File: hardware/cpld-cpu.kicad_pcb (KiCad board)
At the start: 4 copper layers, 264.2 x 190.5 mm, 386 parts, among them J1 Acc, J10 Page, J11 PC_H, J12 Conn_02x16_Odd_Even, J13 Page, J14 Conn_02x16_Odd_Even, J2 X, J3 IR, J4 AXM, J5 Dec, J6 AR, J7 ALU, J8 Index, J9 PC_L, SW1 BTN0, SW2 BTN0, SW3 BTN0, U1 Acc, U10 RAM_Page, U11 PC_H, U12 CY62138FV30LL, U13 GPIO_RNG, U2 X, U3 IR, U4 Multiplexer, U5 Decoder, U6 AR, U7 ALU, U8 RAM_Index, U9 PC_L

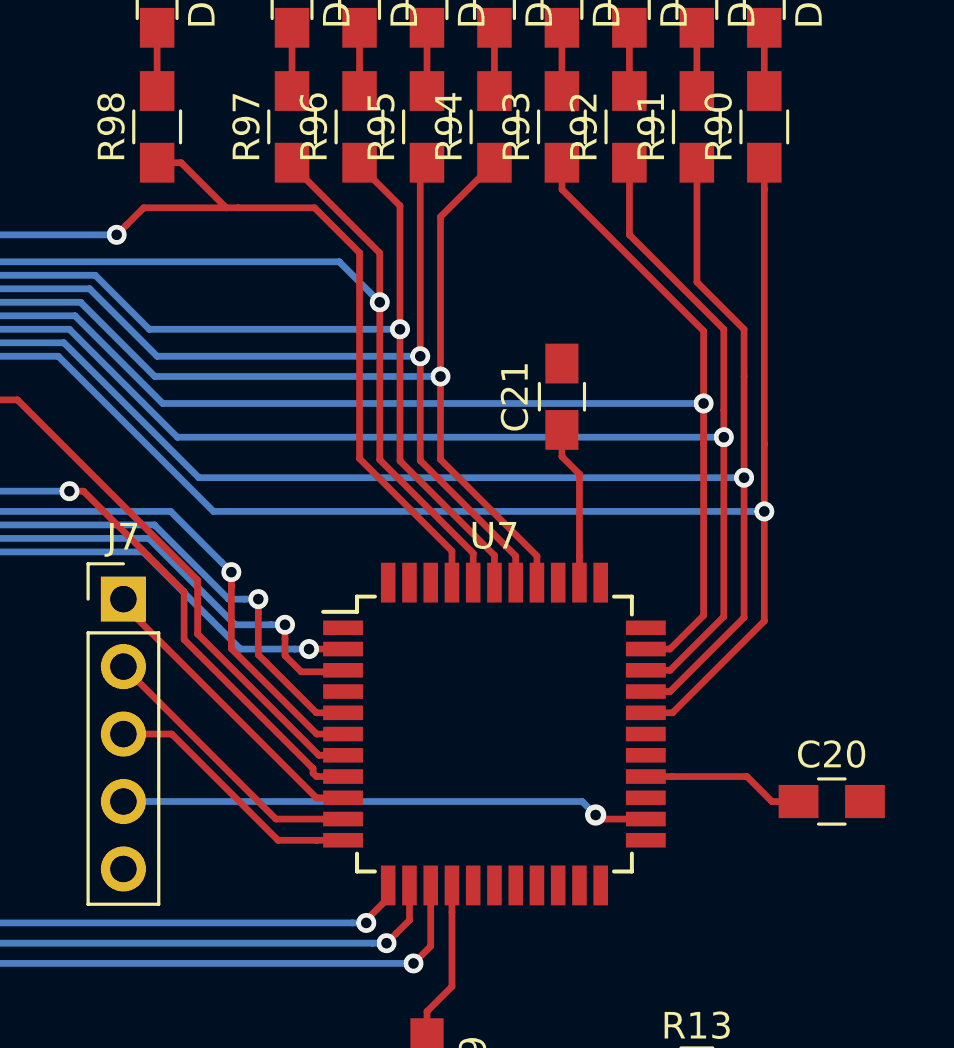
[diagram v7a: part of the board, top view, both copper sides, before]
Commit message: VHDL for alu/decoder/multiplexer
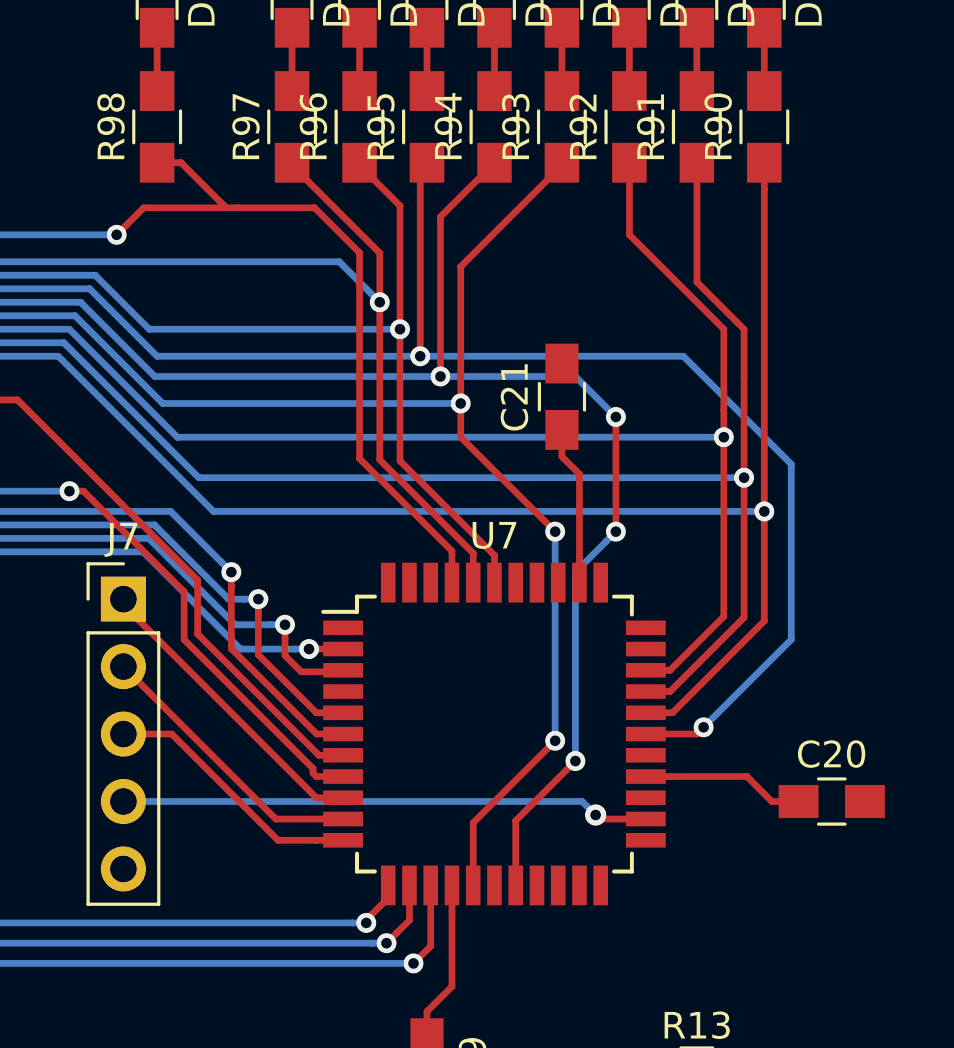
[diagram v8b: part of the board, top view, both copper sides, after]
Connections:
- U7 pad 16: /D0 -> /ALU3
- U7 pad 18: /D1 -> /ALU4
- U7 pad 28: /IR5 -> /ALU5
- U7 pad 32: /ALU3 -> /IR5
- U7 pad 37: /ALU4 -> /D0
- U7 pad 38: /ALU5 -> /D1
- U7 pad 43: /ALU_OE -> /ALU_WE
- U7 pad 44: /ALU_WE -> /ALU_OE
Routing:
- net /ALU5: track 199.3 -> 218.5 mm, vias 4 -> 5
- net /ALU4: track 198.1 -> 215.2 mm, vias 4 -> 7
- net /ALU3: track 209.4 -> 209.9 mm, vias 4 -> 6
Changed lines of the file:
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@@
     (thickness 1.6)
     (drawings 142)
-    (tracks 1644)
+    (tracks 1659)
     (zones 0)
     (modules 386)
@@
       (net 2 VCC))
     (pad 16 smd rect (at -0.8 5.7 90) (size 1.5 0.55) (layers F.Cu F.Paste F.Mask)
-      (net 125 /D0))
+      (net 165 /ALU3))
     (pad 17 smd rect (at 0 5.7 90) (size 1.5 0.55) (layers F.Cu F.Paste F.Mask)
       (net 1 GND))
     (pad 18 smd rect (at 0.8 5.7 90) (size 1.5 0.55) (layers F.Cu F.Paste F.Mask)
-      (net 124 /D1))
+      (net 166 /ALU4))
     (pad 19 smd rect (at 1.6 5.7 90) (size 1.5 0.55) (layers F.Cu F.Paste F.Mask)
       (net 126 /D2))
@@
       (net 131 /D7))
     (pad 28 smd rect (at 5.7 0) (size 1.5 0.55) (layers F.Cu F.Paste F.Mask)
-      (net 104 /IR5))
+      (net 167 /ALU5))
     (pad 29 smd rect (at 5.7 -0.8) (size 1.5 0.55) (layers F.Cu F.Paste F.Mask)
       (net 162 /ALU0))
@@
       (net 164 /ALU2))
     (pad 32 smd rect (at 5.7 -3.2) (size 1.5 0.55) (layers F.Cu F.Paste F.Mask)
-      (net 165 /ALU3))
+      (net 104 /IR5))
     (pad 33 smd rect (at 5.7 -4) (size 1.5 0.55) (layers F.Cu F.Paste F.Mask)
       (net 171 /RST))
@@
       (net 461 "Net-(U7-Pad36)"))
     (pad 37 smd rect (at 1.6 -5.7 90) (size 1.5 0.55) (layers F.Cu F.Paste F.Mask)
-      (net 166 /ALU4))
+      (net 125 /D0))
     (pad 38 smd rect (at 0.8 -5.7 90) (size 1.5 0.55) (layers F.Cu F.Paste F.Mask)
-      (net 167 /ALU5))
+      (net 124 /D1))
     (pad 39 smd rect (at 0 -5.7 90) (size 1.5 0.55) (layers F.Cu F.Paste F.Mask)
       (net 168 /ALU6))
@@
       (net 462 "Net-(U7-Pad42)"))
     (pad 43 smd rect (at -3.2 -5.7 90) (size 1.5 0.55) (layers F.Cu F.Paste F.Mask)
-      (net 192 /ALU_OE))
-    (pad 44 smd rect (at -4 -5.7 90) (size 1.5 0.55) (layers F.Cu F.Paste F.Mask)
       (net 191 /ALU_WE))
+    (pad 44 smd rect (at -4 -5.7 90) (size 1.5 0.55) (layers F.Cu F.Paste F.Mask)
+      (net 192 /ALU_OE))
     (model ${KISYS3DMOD}/Housings_QFP.3dshapes/TQFP-44_10x10mm_Pitch0.8mm.wrl
       (at (xyz 0 0 0))
@@
   (segment (start 32.4 120.976001) (end 32.4 121.12) (width 0.254) (layer F.Cu) (net 164))
   (segment (start 28.956 118.586802) (end 31.345199 120.976001) (width 0.254) (layer F.Cu) (net 164))
-  (segment (start 121.922916 37.914) (end 121.922916 36.91) (width 0.254) (layer F.Cu) (net 165))
-  (segment (start 127.254 43.245084) (end 121.922916 37.914) (width 0.254) (layer F.Cu) (net 165))
-  (segment (start 125.08 55.22) (end 125.990802 55.22) (width 0.254) (layer F.Cu) (net 165))
-  (segment (start 125.990802 55.22) (end 127.254 53.956802) (width 0.254) (layer F.Cu) (net 165))
-  (via (at 127.254 45.974) (size 0.75) (drill 0.4) (layers F.Cu B.Cu) (net 165))
-  (segment (start 127.254 47.244) (end 127.254 47.498) (width 0.254) (layer F.Cu) (net 165))
-  (segment (start 127.254 47.244) (end 127.254 43.245084) (width 0.254) (layer F.Cu) (net 165))
-  (segment (start 127.254 53.956802) (end 127.254 47.498) (width 0.254) (layer F.Cu) (net 165))
-  (segment (start 106.890432 45.974) (end 103.588412 42.67198) (width 0.254) (layer B.Cu) (net 165))
-  (segment (start 29.107136 42.671982) (end 28.267389 43.511729) (width 0.254) (layer B.Cu) (net 165))
-  (segment (start 103.588412 42.67198) (end 29.107136 42.671982) (width 0.254) (layer B.Cu) (net 165))
-  (segment (start 28.267389 43.616744) (end 28.267389 44.147074) (width 0.254) (layer B.Cu) (net 165))
   (via (at 28.267389 44.147074) (size 0.75) (drill 0.4) (layers F.Cu B.Cu) (net 165))
-  (segment (start 28.267389 43.511729) (end 28.267389 43.616744) (width 0.254) (layer B.Cu) (net 165))
-  (segment (start 127.254 45.974) (end 106.890432 45.974) (width 0.254) (layer B.Cu) (net 165))
   (segment (start 28.429444 44.309129) (end 28.267389 44.147074) (width 0.254) (layer F.Cu) (net 165))
   (segment (start 28.429444 45.354696) (end 28.429444 44.309129) (width 0.254) (layer F.Cu) (net 165))
@@
   (segment (start 31.268999 121.484011) (end 31.134775 121.484011) (width 0.254) (layer F.Cu) (net 165))
   (segment (start 32.256001 121.776001) (end 31.345199 121.776001) (width 0.254) (layer F.Cu) (net 165))
-  (segment (start 120.98 51.716) (end 120.98 52.72) (width 0.254) (layer F.Cu) (net 166))
-  (segment (start 117.348 48.084) (end 120.98 51.716) (width 0.254) (layer F.Cu) (net 166))
+  (segment (start 28.267389 43.616744) (end 28.267389 44.147074) (width 0.254) (layer B.Cu) (net 165))
+  (segment (start 118.11 45.974) (end 106.890432 45.974) (width 0.254) (layer B.Cu) (net 165))
+  (segment (start 106.890432 45.974) (end 103.588412 42.67198) (width 0.254) (layer B.Cu) (net 165))
+  (via (at 118.11 45.974) (size 0.75) (drill 0.4) (layers F.Cu B.Cu) (net 165))
+  (segment (start 29.107136 42.671982) (end 28.267389 43.511729) (width 0.254) (layer B.Cu) (net 165))
+  (segment (start 28.267389 43.511729) (end 28.267389 43.616744) (width 0.254) (layer B.Cu) (net 165))
+  (segment (start 103.588412 42.67198) (end 29.107136 42.671982) (width 0.254) (layer B.Cu) (net 165))
+  (segment (start 118.11 40.82) (end 118.11 45.974) (width 0.254) (layer F.Cu) (net 165))
+  (segment (start 121.92 36.91) (end 121.92 37.01) (width 0.254) (layer F.Cu) (net 165))
+  (segment (start 121.92 37.01) (end 118.11 40.82) (width 0.254) (layer F.Cu) (net 165))
+  (via (at 121.666 50.8) (size 0.75) (drill 0.4) (layers F.Cu B.Cu) (net 165))
+  (segment (start 118.11 45.974) (end 118.11 47.244) (width 0.254) (layer F.Cu) (net 165))
+  (segment (start 118.11 47.244) (end 121.666 50.8) (width 0.254) (layer F.Cu) (net 165))
+  (segment (start 121.666 50.8) (end 121.666 58.674) (width 0.254) (layer B.Cu) (net 165))
+  (via (at 121.666 58.674) (size 0.75) (drill 0.4) (layers F.Cu B.Cu) (net 165))
+  (segment (start 118.58 61.76) (end 118.58 64.12) (width 0.254) (layer F.Cu) (net 165))
+  (segment (start 121.666 58.674) (end 118.58 61.76) (width 0.254) (layer F.Cu) (net 165))
   (segment (start 119.382916 36.91) (end 117.348 38.944916) (width 0.254) (layer F.Cu) (net 166))
   (via (at 117.348 44.958) (size 0.75) (drill 0.4) (layers F.Cu B.Cu) (net 166))
   (segment (start 117.348 38.944916) (end 117.348 44.958) (width 0.254) (layer F.Cu) (net 166))
-  (segment (start 117.348 44.958) (end 117.348 48.084) (width 0.254) (layer F.Cu) (net 166))
   (segment (start 117.348 44.958) (end 106.592866 44.958) (width 0.254) (layer B.Cu) (net 166))
   (segment (start 28.896711 42.163973) (end 27.178 43.882684) (width 0.254) (layer B.Cu) (net 166))
@@
   (segment (start 27.686 57.912) (end 27.686 63.5) (width 0.254) (layer B.Cu) (net 166))
   (segment (start 27.686 64.516) (end 27.686 71.504709) (width 0.254) (layer F.Cu) (net 166))
-  (segment (start 120.18 51.716) (end 120.18 52.72) (width 0.254) (layer F.Cu) (net 167))
-  (segment (start 116.586 48.122) (end 120.18 51.716) (width 0.254) (layer F.Cu) (net 167))
+  (segment (start 117.348 44.958) (end 122.428 44.958) (width 0.254) (layer B.Cu) (net 166))
+  (via (at 123.952 46.482) (size 0.75) (drill 0.4) (layers F.Cu B.Cu) (net 166))
+  (segment (start 122.428 44.958) (end 123.952 46.482) (width 0.254) (layer B.Cu) (net 166))
+  (via (at 123.952 50.8) (size 0.75) (drill 0.4) (layers F.Cu B.Cu) (net 166))
+  (segment (start 123.952 46.482) (end 123.952 50.8) (width 0.254) (layer F.Cu) (net 166))
+  (segment (start 123.952 50.8) (end 123.577001 51.174999) (width 0.254) (layer B.Cu) (net 166))
+  (via (at 122.428 59.436) (size 0.75) (drill 0.4) (layers F.Cu B.Cu) (net 166))
+  (segment (start 123.577001 51.174999) (end 122.428 52.324) (width 0.254) (layer B.Cu) (net 166))
+  (segment (start 122.428 52.324) (end 122.428 59.436) (width 0.254) (layer B.Cu) (net 166))
+  (segment (start 120.18 61.684) (end 120.18 64.12) (width 0.254) (layer F.Cu) (net 166))
+  (segment (start 122.428 59.436) (end 120.18 61.684) (width 0.254) (layer F.Cu) (net 166))
   (segment (start 116.842916 36.91) (end 116.586 37.166916) (width 0.254) (layer F.Cu) (net 167))
   (segment (start 116.586 37.166916) (end 116.586 44.196) (width 0.254) (layer F.Cu) (net 167))
   (via (at 116.586 44.196) (size 0.75) (drill 0.4) (layers F.Cu B.Cu) (net 167))
-  (segment (start 116.586 44.196) (end 116.586 48.122) (width 0.254) (layer F.Cu) (net 167))
   (via (at 26.162014 44.958) (size 0.75) (drill 0.4) (layers F.Cu B.Cu) (net 167))
   (segment (start 26.162014 44.180236) (end 26.162014 44.42767) (width 0.254) (layer B.Cu) (net 167))
@@
   (segment (start 26.923989 119.047989) (end 26.923989 116.324595) (width 0.254) (layer F.Cu) (net 167))
   (segment (start 26.923989 116.324595) (end 25.892935 115.293541) (width 0.254) (layer F.Cu) (net 167))
+  (segment (start 116.586 44.196) (end 126.492 44.196) (width 0.254) (layer B.Cu) (net 167))
+  (segment (start 126.492 44.196) (end 130.556 48.26) (width 0.254) (layer B.Cu) (net 167))
+  (via (at 127.254 58.166) (size 0.75) (drill 0.4) (layers F.Cu B.Cu) (net 167))
+  (segment (start 130.556 48.26) (end 130.556 54.864) (width 0.254) (layer B.Cu) (net 167))
+  (segment (start 130.556 54.864) (end 127.254 58.166) (width 0.254) (layer B.Cu) (net 167))
+  (segment (start 127 58.42) (end 125.08 58.42) (width 0.254) (layer F.Cu) (net 167))
+  (segment (start 127.254 58.166) (end 127 58.42) (width 0.254) (layer F.Cu) (net 167))
   (segment (start 114.302916 37.01) (end 114.302916 36.91) (width 0.254) (layer F.Cu) (net 168))
   (segment (start 115.824 38.531084) (end 114.302916 37.01) (width 0.254) (layer F.Cu) (net 168))
